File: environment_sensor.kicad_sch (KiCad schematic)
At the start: 123 parts, among them J17 USB-C_GCT_USB4145-03-0070-C, J18 JST_SH_1x4_SM04B-SRSS-TB-LF-SN, J20 JST_SH_1x4_SM04B-SRSS-TB-LF-SN, U11 FT4232H_VQFN, U27 AP7370-33SA-7, U28 STM32G474CET6, U29 MB85RC1MTPNF-G, U30 SHT45, U31 BME280, Y2 Resonator_12MHz_ABM3B, Y3 Resonator_32.768kHz_ECX-31B, Y4 Resonator_8MHz_ABM3B

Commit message: [#61047] Perform kmake DNP and update symbols
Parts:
- C104, C105, C106, C56, C57, C59, C60, C62, C63, C64, C65, C67, C68, C69, C70, C71, C72, C73, C74, C75, C76, C77, C78, C79, C80, C81, C82, C83, C84, C85, C86, C87, C88, C89, C90, C91, C92, C93, C94, C95, D36, D37, D38, D39, D42, D44, FB13, FB14, FB15, FB16, FB17, LD1, LD2, R251, R253, R254, R255, R256, R257, R258, R260, R261, R264, R265, R266, R269, R271, R272, R277, R278, R279, R280, R281, R282, R283, R284, R285, R286, R287, R288, R289, R302, Y2, Y3, Y4: Public False -> (none)
- H10, H11, H12, R250, R252, R259, R262, R263, R267, R268, R270, R273, R274, R275, R276, R290: DNP DNP -> (none); Public False -> (none); now not fitted
- TP6, TP60, TP61, TP62, TP63, TP64, TP65, TP66, TP67: Public False -> (none); now left out of the parts list

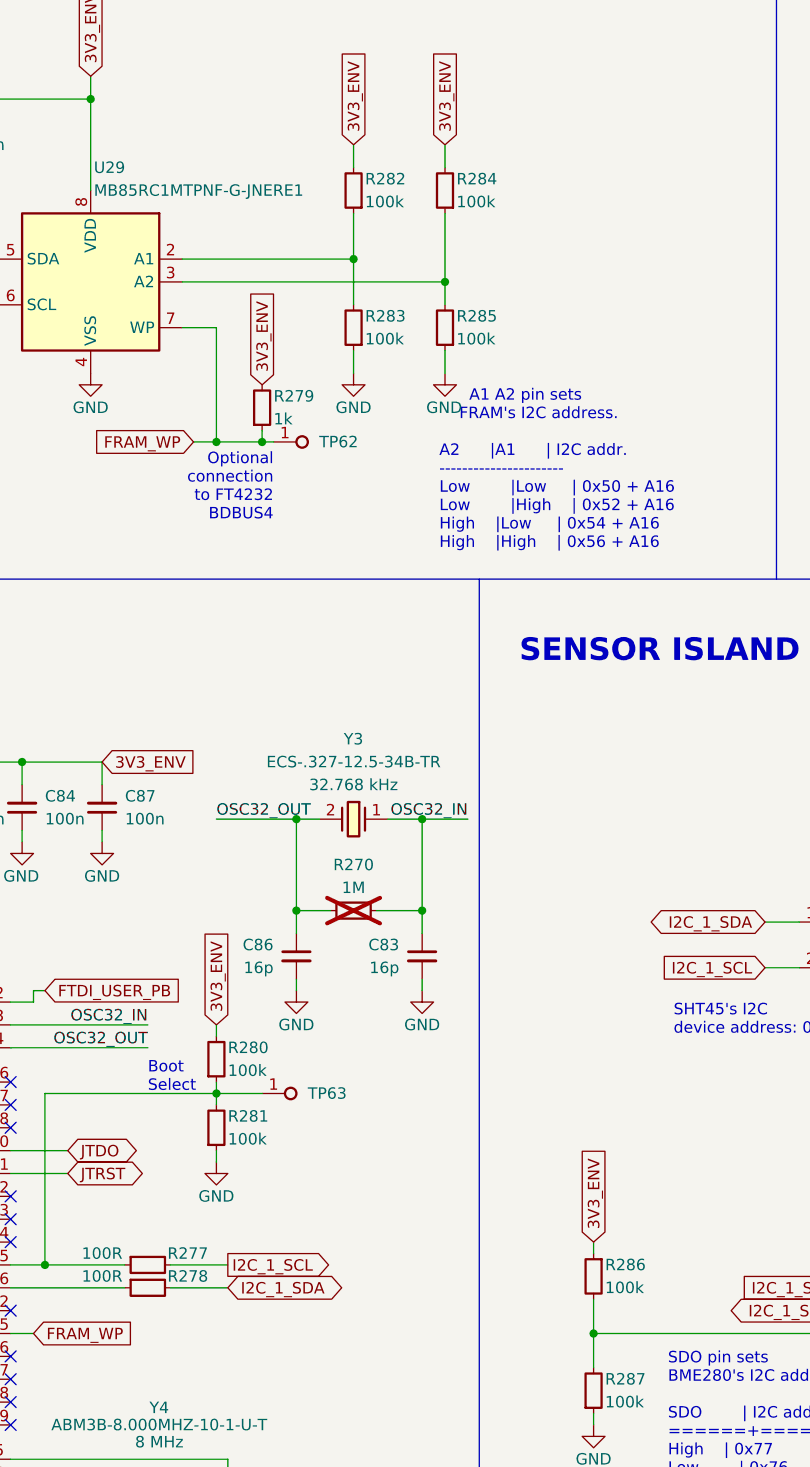
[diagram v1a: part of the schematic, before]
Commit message: [#61047] Mark R286, R282, R284, R281 as DNP
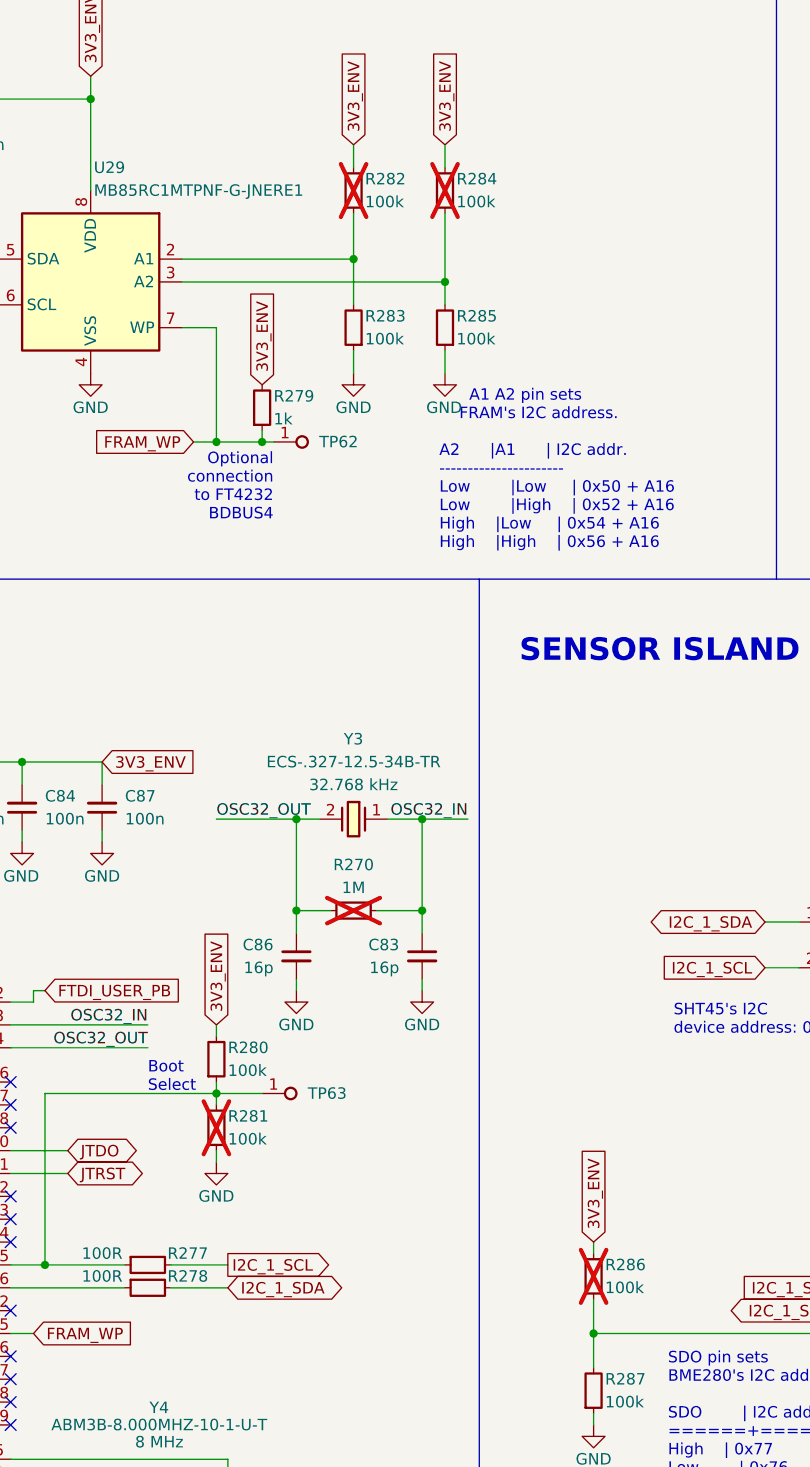
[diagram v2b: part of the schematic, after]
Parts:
- R281, R282, R284, R286: now not fitted
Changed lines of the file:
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@@
   )
   (symbol (lib_id "antmicroResistors0402:R_100k_0402") (at 306.07 46.99 270) (mirror x) (unit 1)
-    (in_bom yes) (on_board yes) (dnp no)
+    (in_bom yes) (on_board yes) (dnp yes)
     (property "Reference" "R282" (at 307.34 43.18 90)
       (effects (font (size 1.27 1.27) (thickness 0.15)) (justify left))
@@
   )
   (symbol (lib_id "antmicroResistors0402:R_100k_0402") (at 332.74 162.56 270) (unit 1)
-    (in_bom yes) (on_board yes) (dnp no)
+    (in_bom yes) (on_board yes) (dnp yes)
     (property "Reference" "R286" (at 334.01 163.83 90)
       (effects (font (size 1.27 1.27) (thickness 0.15)) (justify left))
@@
   )
   (symbol (lib_id "antmicroResistors0402:R_100k_0402") (at 290.83 151.13 90) (unit 1)
-    (in_bom yes) (on_board yes) (dnp no)
+    (in_bom yes) (on_board yes) (dnp yes)
     (property "Reference" "R281" (at 292.1 147.32 90)
       (effects (font (size 1.27 1.27) (thickness 0.15)) (justify right))
@@
   )
   (symbol (lib_id "antmicroResistors0402:R_100k_0402") (at 316.23 46.99 270) (mirror x) (unit 1)
-    (in_bom yes) (on_board yes) (dnp no)
+    (in_bom yes) (on_board yes) (dnp yes)
     (property "Reference" "R284" (at 317.5 43.18 90)
       (effects (font (size 1.27 1.27) (thickness 0.15)) (justify left))

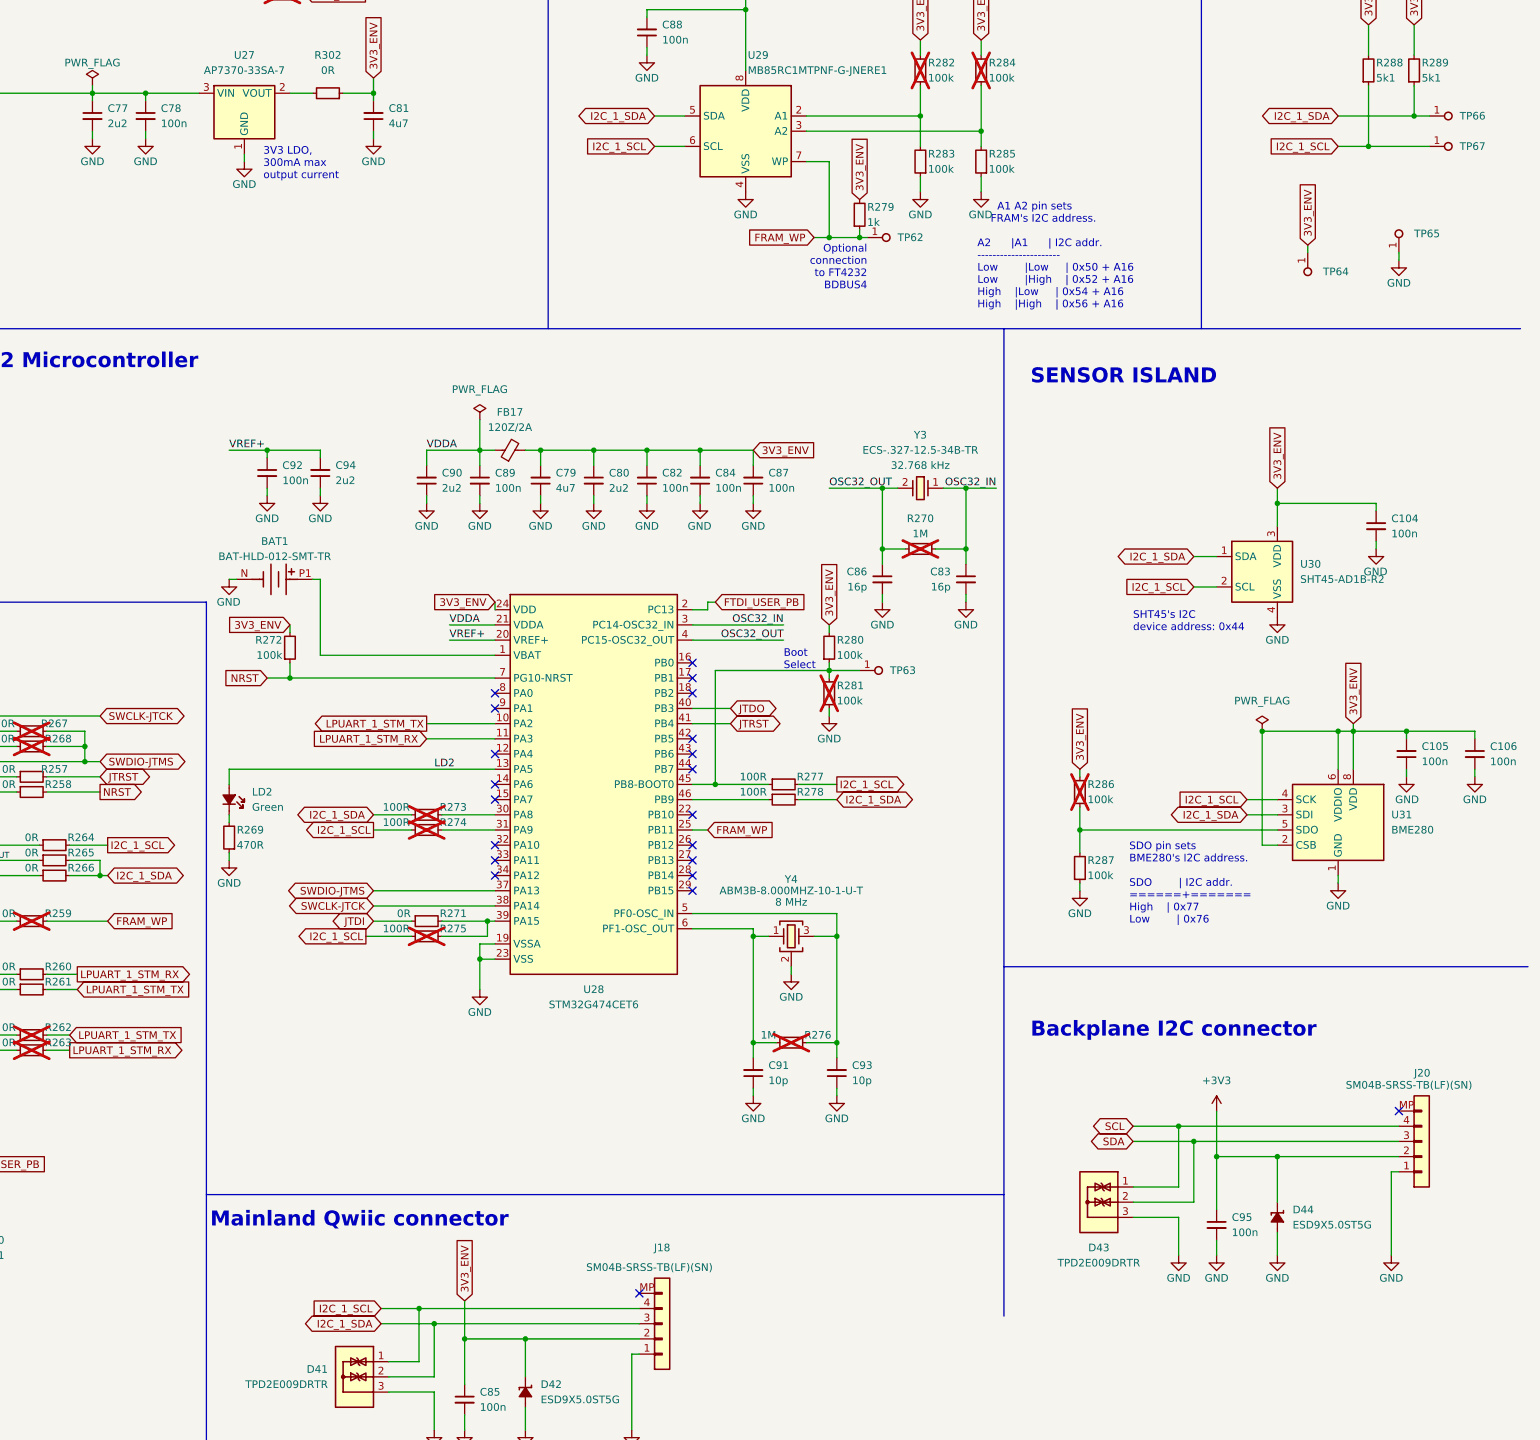
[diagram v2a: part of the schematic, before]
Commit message: [#62160] Rm U2, J19, J20 and its passives
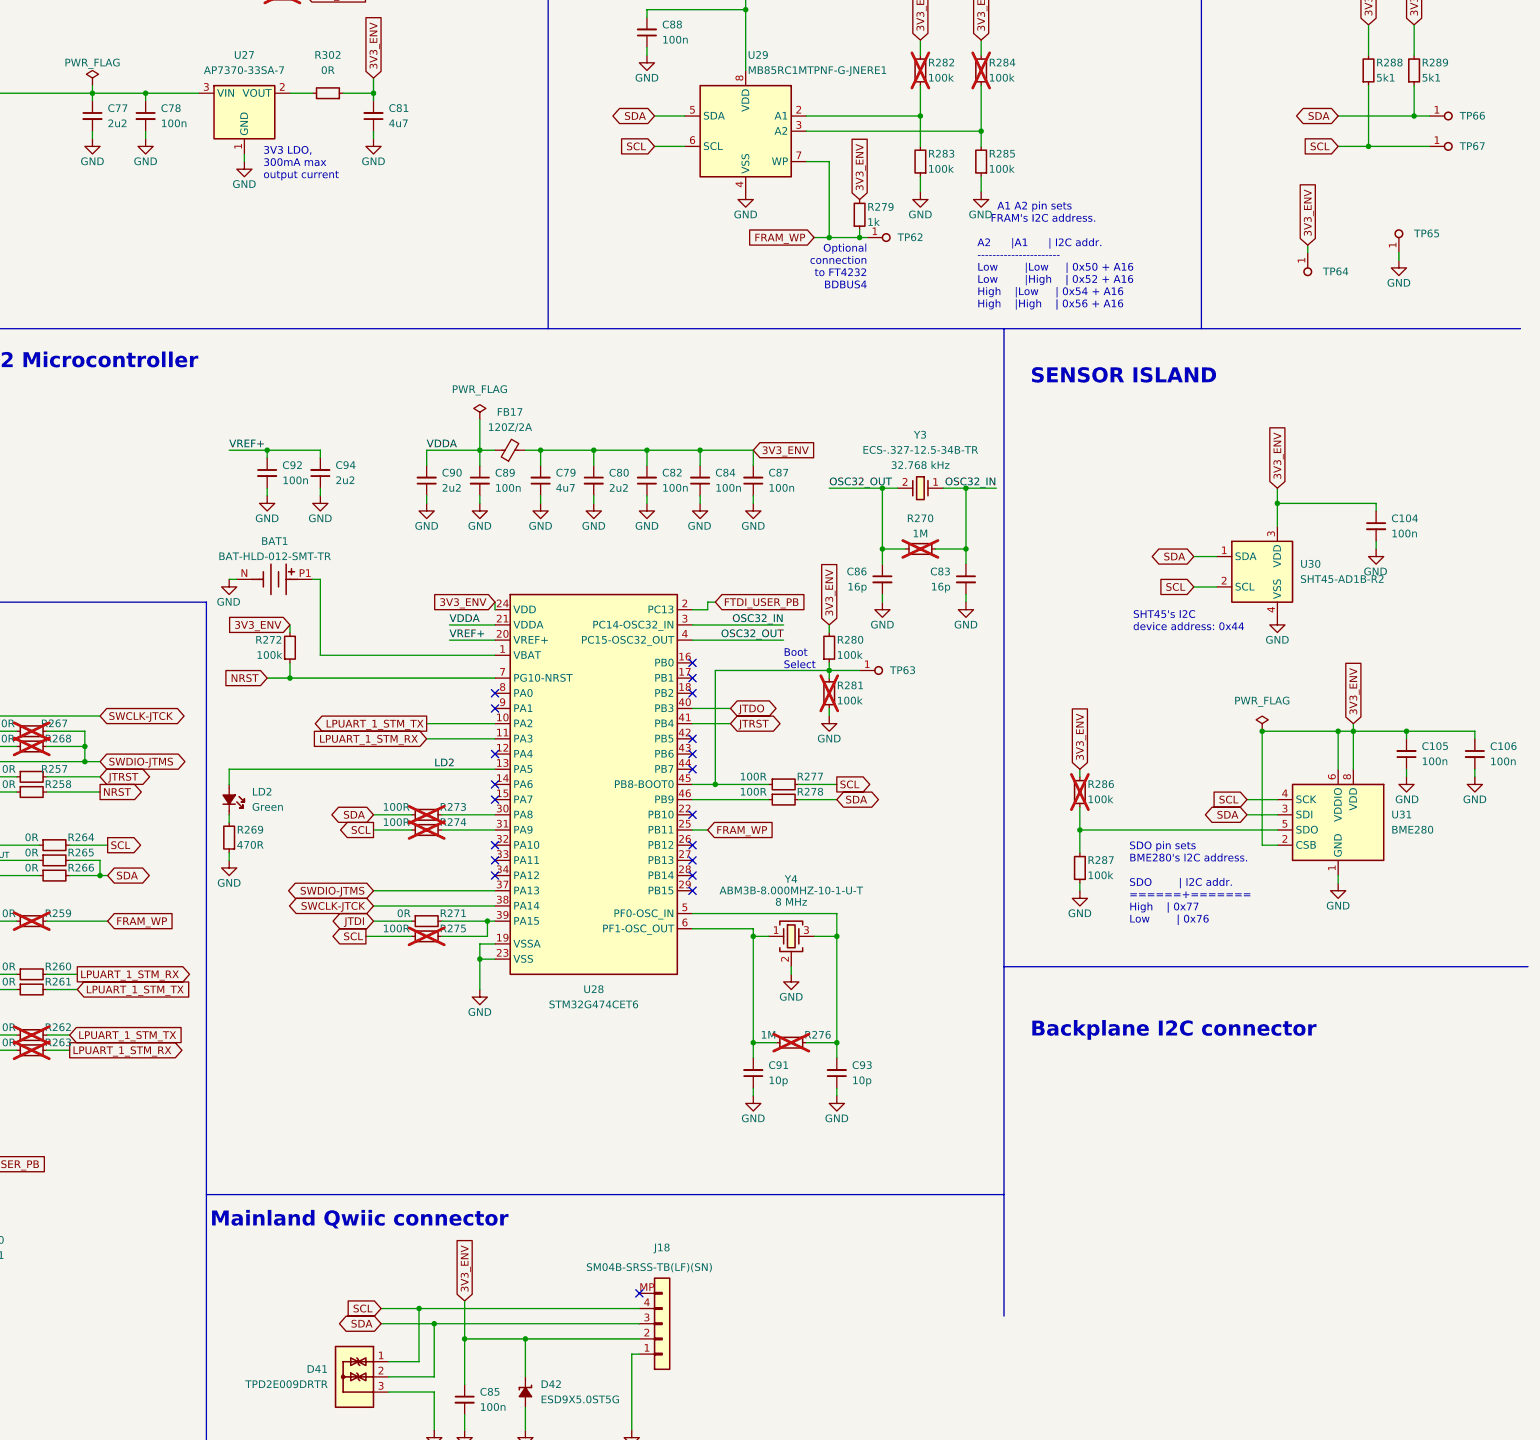
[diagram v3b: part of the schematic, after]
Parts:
- removed C95: C_100n_0402, antmicro-footprints:C_0402_1005Metric, symbol antmicroCapacitors0402:C_100n_0402
- removed D43: TPD2E009_SOT-9X3, antmicro-footprints:SOT-723, symbol antmicroTVSDiodes:TPD2E009_SOT-9X3
- removed D44: ESD9X5.0ST5G, antmicro-footprints:SOD-923, symbol antmicroTVSDiodes:ESD9X5.0ST5G
- removed J20: JST_SH_1x4_SM04B-SRSS-TB-LF-SN, antmicro-footprints:Conn_JST_SH_1x4_SM04B-SRSS-TB-LF-SN, symbol antmicroWire2BoardConnectors:JST_SH_1x4_SM04B-SRSS-TB-LF-SN
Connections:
- net I2C_1_SCL is gone; now on net SCL: D41.1, J18.4, R264.2, R274.2, R275.2, R277.2, R288.1, TP67.1, U29.6 (SCL), U30.2 (SCL), U31.4 (SCK)
- net I2C_1_SDA is gone; now on net SDA: D41.2, J18.3, R265.2, R266.2, R273.2, R278.2, R289.1, TP66.1, U29.5 (SDA), U30.1 (SDA), U31.3 (SDI)
- no-connect marks 48 -> 47

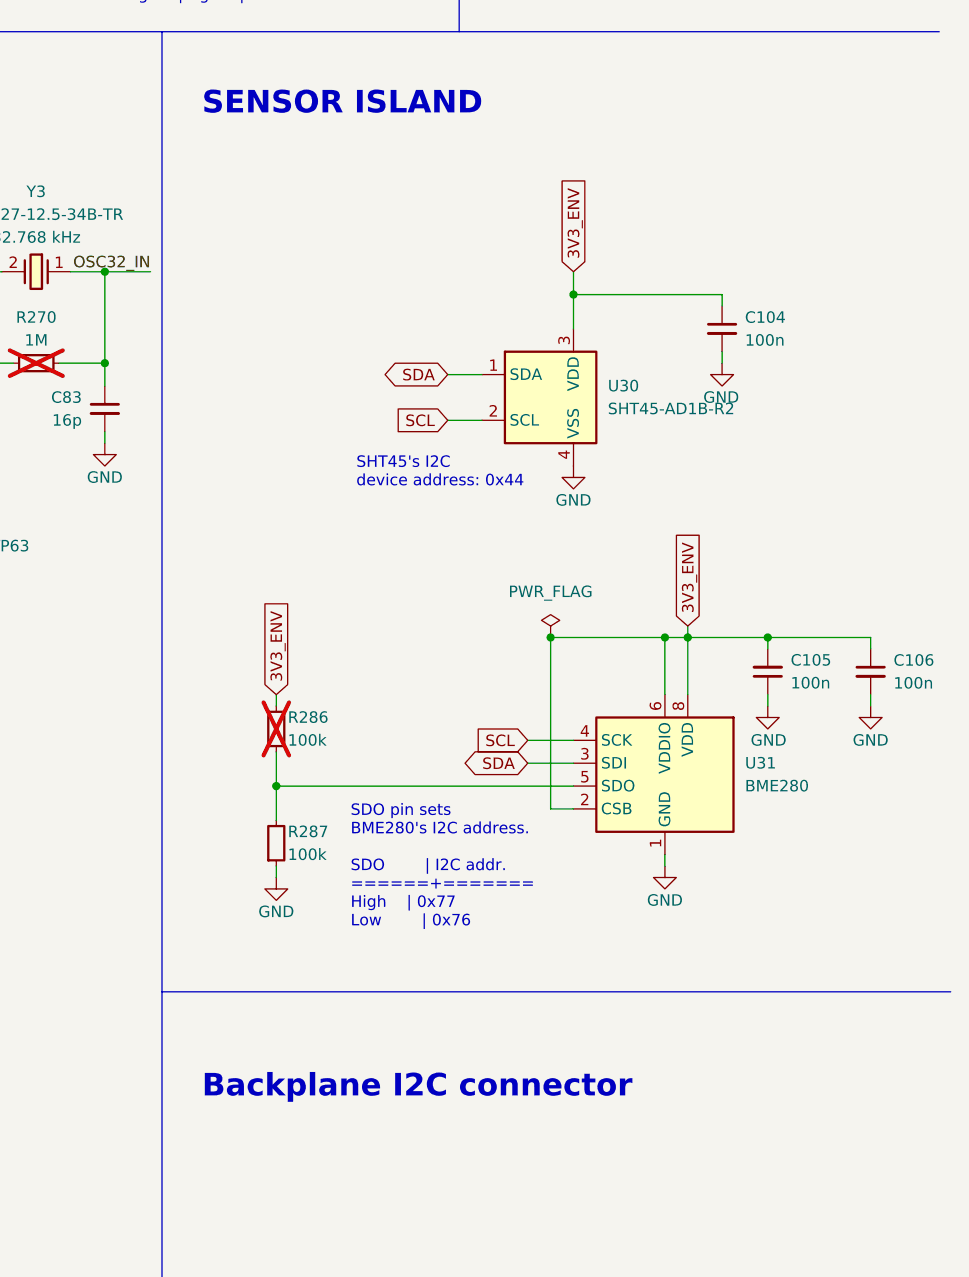
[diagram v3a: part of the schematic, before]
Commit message: [#62160] Rm U2 FTDI leftovers from schematic
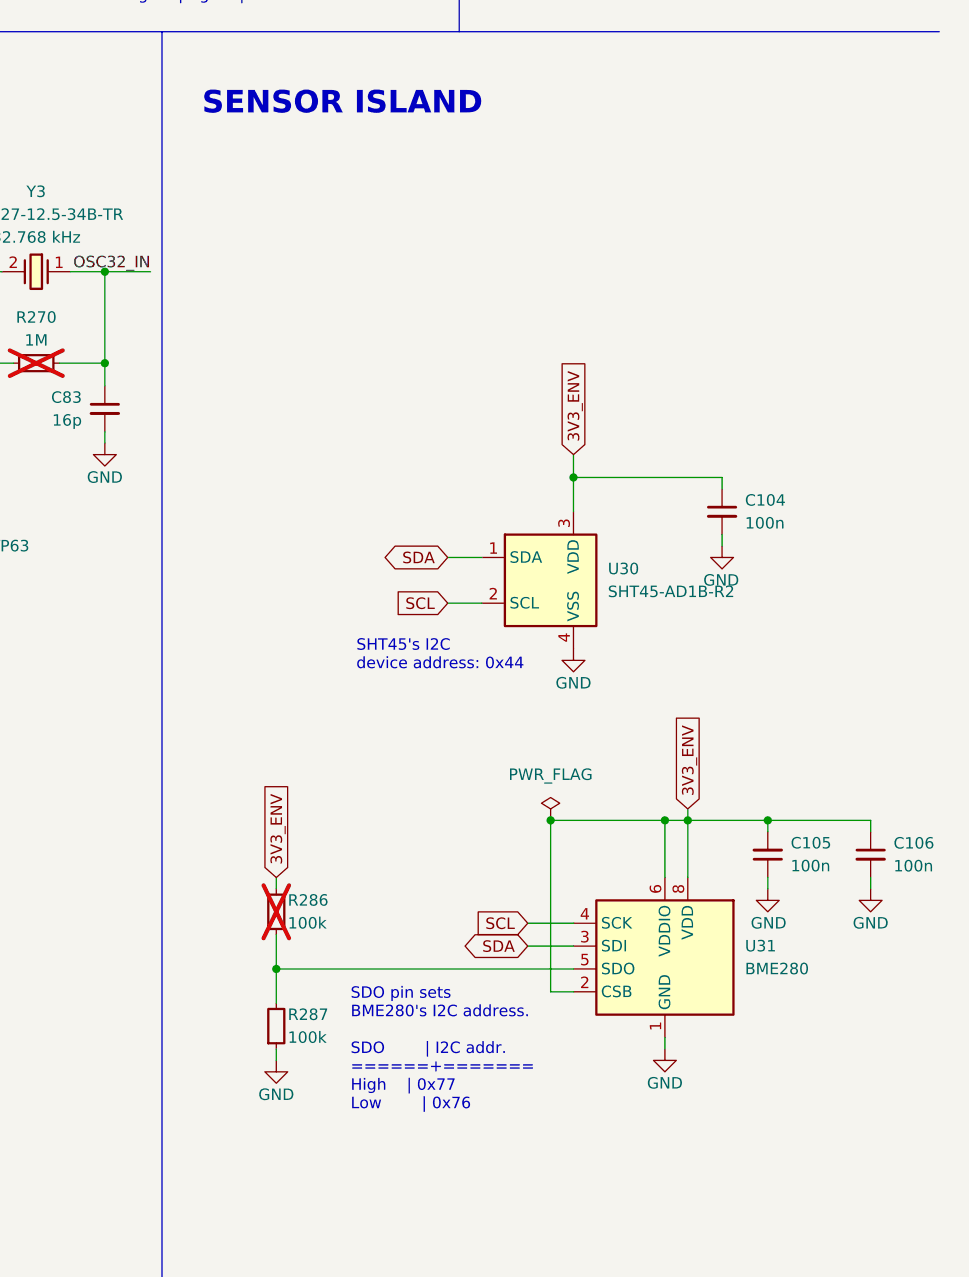
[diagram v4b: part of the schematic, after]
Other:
- note removed: "Backplane I2C connector"
- moved on the sheet: C104, C105, C106, R286, R287, U30, U31
